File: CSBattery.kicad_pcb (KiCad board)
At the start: 2 copper layers, 30 parts, among them CON101 USB-MICRO-B, P101 USB5v, P102 ChgV, P103 Battery, P104 uController, P105 Gnd, P106 PwrOut, Q101 BC817, Q102 BC817, SW101 PwrOutOn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

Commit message: amended schematic to incorporate a gnd reference line for the uController signals
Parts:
- P104: footprint Pin_Headers:Pin_Header_Straight_1x02 -> Pin_Headers:Pin_Header_Straight_1x03
- moved P104 38.5 mm to (203.0, 134.2)
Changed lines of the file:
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@@
 (kicad_pcb (version 4) (host pcbnew "(2015-04-23 BZR 5622)-product")
   (general
-    (links 58)
-    (no_connects 58)
+    (links 59)
+    (no_connects 59)
     (area 0 0 0 0)
     (thickness 1.6)
@@
     )
   )
-  (module Pin_Headers:Pin_Header_Straight_1x02 (layer F.Cu)
-    (at 165.839268 124.2646)
-    (descr "Through hole pin header")
-    (tags "pin header")
-    (fp_text reference P104 (at 0 -5.1) (layer F.SilkS)
-      (effects (font (size 1 1) (thickness 0.15)))
-    )
-    (fp_text value uController (at 0 -3.1) (layer F.Fab)
-      (effects (font (size 1 1) (thickness 0.15)))
-    )
-    (fp_line (start 1.27 1.27) (end 1.27 3.81) (layer F.SilkS) (width 0.15))
-    (fp_line (start 1.55 -1.55) (end 1.55 0) (layer F.SilkS) (width 0.15))
-    (fp_line (start -1.75 -1.75) (end -1.75 4.3) (layer F.CrtYd) (width 0.05))
-    (fp_line (start 1.75 -1.75) (end 1.75 4.3) (layer F.CrtYd) (width 0.05))
-    (fp_line (start -1.75 -1.75) (end 1.75 -1.75) (layer F.CrtYd) (width 0.05))
-    (fp_line (start -1.75 4.3) (end 1.75 4.3) (layer F.CrtYd) (width 0.05))
-    (fp_line (start 1.27 1.27) (end -1.27 1.27) (layer F.SilkS) (width 0.15))
-    (fp_line (start -1.55 0) (end -1.55 -1.55) (layer F.SilkS) (width 0.15))
-    (fp_line (start -1.55 -1.55) (end 1.55 -1.55) (layer F.SilkS) (width 0.15))
-    (fp_line (start -1.27 1.27) (end -1.27 3.81) (layer F.SilkS) (width 0.15))
-    (fp_line (start -1.27 3.81) (end 1.27 3.81) (layer F.SilkS) (width 0.15))
-    (pad 1 thru_hole rect (at 0 0) (size 2.032 2.032) (drill 1.016) (layers *.Cu *.Mask F.SilkS)
-      (net 11 "Net-(P104-Pad1)"))
-    (pad 2 thru_hole oval (at 0 2.54) (size 2.032 2.032) (drill 1.016) (layers *.Cu *.Mask F.SilkS)
-      (net 12 "Net-(P104-Pad2)"))
-    (model Pin_Headers.3dshapes/Pin_Header_Straight_1x02.wrl
-      (at (xyz 0 -0.05 0))
-      (scale (xyz 1 1 1))
-      (rotate (xyz 0 0 90))
-    )
-  )
   (module Measurement_Points:Measurement_Point_Round-TH_Small (layer F.Cu)
     (at 185.601171 110.9546)
@@
       (net 4 "Net-(C103-Pad1)"))
   )
+  (module Pin_Headers:Pin_Header_Straight_1x03 (layer F.Cu)
+    (at 203.0476 134.1501)
+    (descr "Through hole pin header")
+    (tags "pin header")
+    (fp_text reference P104 (at 0 -5.1) (layer F.SilkS)
+      (effects (font (size 1 1) (thickness 0.15)))
+    )
+    (fp_text value uController (at 0 -3.1) (layer F.Fab)
+      (effects (font (size 1 1) (thickness 0.15)))
+    )
+    (fp_line (start -1.75 -1.75) (end -1.75 6.85) (layer F.CrtYd) (width 0.05))
+    (fp_line (start 1.75 -1.75) (end 1.75 6.85) (layer F.CrtYd) (width 0.05))
+    (fp_line (start -1.75 -1.75) (end 1.75 -1.75) (layer F.CrtYd) (width 0.05))
+    (fp_line (start -1.75 6.85) (end 1.75 6.85) (layer F.CrtYd) (width 0.05))
+    (fp_line (start -1.27 1.27) (end -1.27 6.35) (layer F.SilkS) (width 0.15))
+    (fp_line (start -1.27 6.35) (end 1.27 6.35) (layer F.SilkS) (width 0.15))
+    (fp_line (start 1.27 6.35) (end 1.27 1.27) (layer F.SilkS) (width 0.15))
+    (fp_line (start 1.55 -1.55) (end 1.55 0) (layer F.SilkS) (width 0.15))
+    (fp_line (start 1.27 1.27) (end -1.27 1.27) (layer F.SilkS) (width 0.15))
+    (fp_line (start -1.55 0) (end -1.55 -1.55) (layer F.SilkS) (width 0.15))
+    (fp_line (start -1.55 -1.55) (end 1.55 -1.55) (layer F.SilkS) (width 0.15))
+    (pad 1 thru_hole rect (at 0 0) (size 2.032 1.7272) (drill 1.016) (layers *.Cu *.Mask F.SilkS)
+      (net 11 "Net-(P104-Pad1)"))
+    (pad 2 thru_hole oval (at 0 2.54) (size 2.032 1.7272) (drill 1.016) (layers *.Cu *.Mask F.SilkS)
+      (net 12 "Net-(P104-Pad2)"))
+    (pad 3 thru_hole oval (at 0 5.08) (size 2.032 1.7272) (drill 1.016) (layers *.Cu *.Mask F.SilkS)
+      (net 2 GND))
+    (model Pin_Headers.3dshapes/Pin_Header_Straight_1x03.wrl
+      (at (xyz 0 -0.1 0))
+      (scale (xyz 1 1 1))
+      (rotate (xyz 0 0 90))
+    )
+  )
 )

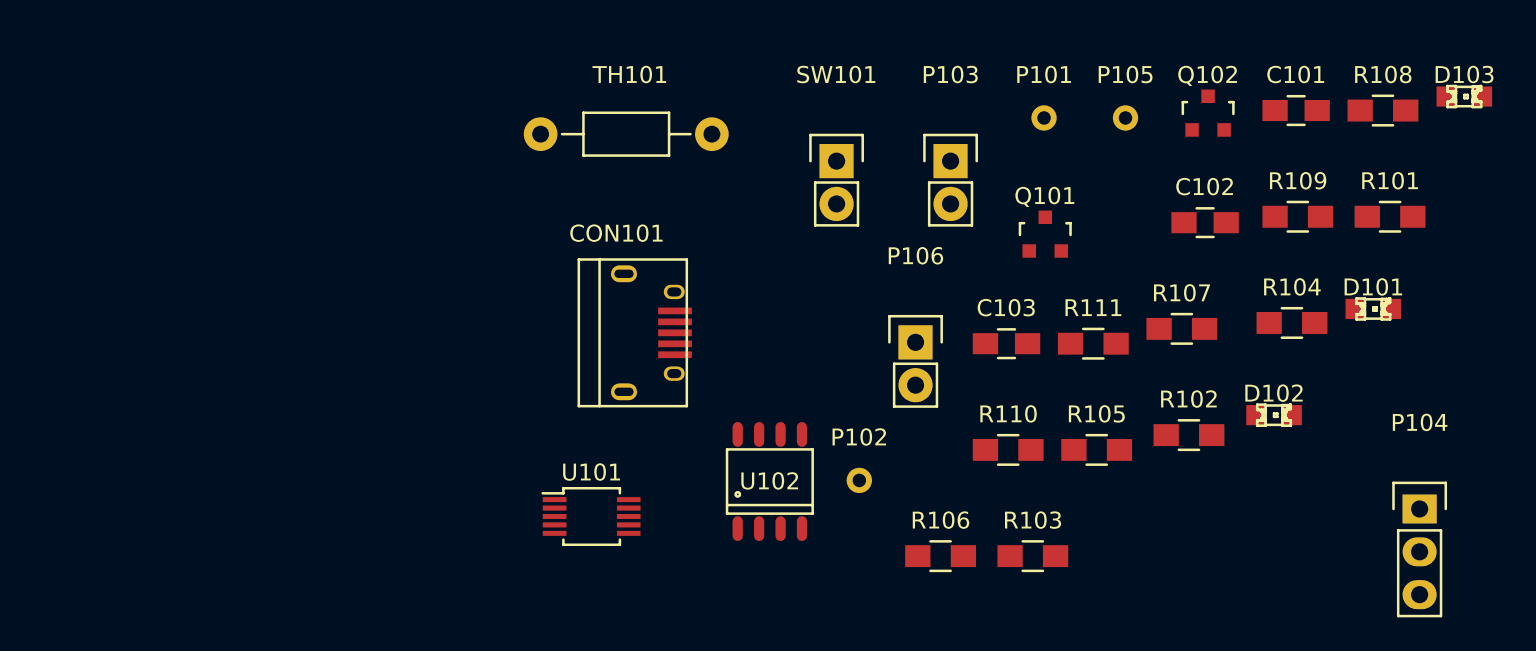
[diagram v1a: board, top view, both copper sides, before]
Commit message: updated schematic to include a flyback schottky diode to protect the circuit from Fan inductance
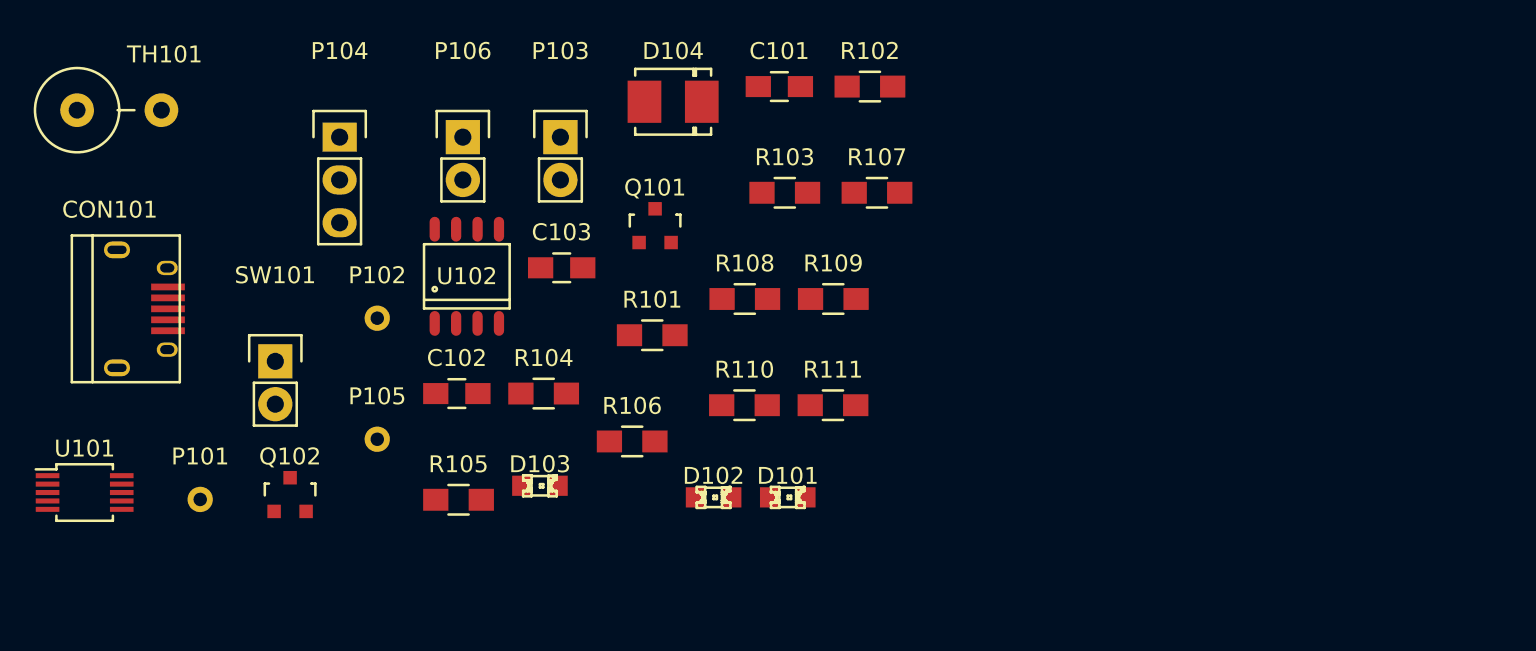
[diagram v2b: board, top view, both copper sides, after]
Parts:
- added D104: B130-13, Diodes_SMD:Diode-DO-214BA, F.Cu at (158.8, 110.0)
- TH101: footprint Resistors_ThroughHole:Resistor_Horizontal_RM10mm -> Resistors_ThroughHole:Resistor_Vertical_RM5mm
- moved P104 67.8 mm to (139.0, 112.1)
- moved D103 59.5 mm to (150.9, 132.8)
- moved Q102 59.0 mm to (136.0, 133.3)
- moved P101 54.9 mm to (130.7, 133.6)
- moved P105 48.3 mm to (141.2, 130.0)
- moved C102 45.5 mm to (145.9, 127.3)
- moved R104 44.6 mm to (151.1, 127.3)
- moved R101 44.3 mm to (157.5, 123.8)
- moved R108 39.5 mm to (163.0, 121.7)
- moved R105 38.0 mm to (146.0, 133.6)
- moved D101 36.5 mm to (165.6, 133.5)
- moved SW101 35.3 mm to (135.2, 125.4)
- moved D102 33.6 mm to (161.2, 133.5)
- moved C101 30.7 mm to (165.1, 109.1)
- moved P102 30.2 mm to (141.2, 122.8)
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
